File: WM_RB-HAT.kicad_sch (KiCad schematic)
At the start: 98 parts, among them J1 Line R, J2 Output Stereo, J3 2x20 Pins, J5 Output Mono, J7 Line L, Q1 BC817, Q2 BFS17A, U1 WM8960, U3 74AHC1G14, U4 MCP1711T-33 /OT, X1 XO32, Y1 24MHz

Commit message: WIP v1.1: SMD migration + input simplification
- Remove differential input stage, simplify jacks
- Migrate to 0603, remove HandSolder footprints
- Add LCSC codes, 4-layer stackup config
- Add SMD libs and design docs
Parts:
- removed C33, C34: 390p, Capacitor_SMD:C_0805_2012Metric_Pad1.18x1.45mm_HandSolder, symbol Device:C_Small
- removed C37, C38: 1u Film P5-7.5mm W<6mm, ArduinoModules:C_Rect_Film_L7.2mm_W5.5mm_P5.00mm_7.5mm_Combo_FKS2_FKP2_MKS2_MKP2, symbol Device:C_Small
- removed FB6, FB7: 220-1k, Inductor_SMD:L_0805_2012Metric_Pad1.15x1.40mm_HandSolder, symbol Device:FerriteBead_Small
- removed J1: Line R, ArduinoModules:Jack_3.5mm_Combo_CUI_SJ1-3525N_Horizontal, symbol Connector_Audio:AudioJack3_SwitchTR
- removed J2: Output Stereo, ArduinoModules:Jack_3.5mm_Combo_CUI_SJ1-3525N_Horizontal, symbol Connector_Audio:AudioJack3_SwitchTR
- removed J5: Output Mono, ArduinoModules:Jack_3.5mm_Combo_CUI_SJ1-3525N_Horizontal, symbol Connector_Audio:AudioJack3_SwitchTR
- removed J7: Line L, ArduinoModules:Jack_3.5mm_Combo_CUI_SJ1-3525N_Horizontal, symbol Connector_Audio:AudioJack3_SwitchTR
- removed JP3: Line, ArduinoModules:SolderJumper-2_P1.3mm_Open_TrianglePad1.0x1.5mm, symbol 0Arduino_Modules:SolderJumper_2_Open
- removed R25: 1k, Resistor_SMD:R_0805_2012Metric_Pad1.20x1.40mm_HandSolder, symbol Device:R_Small_US
- removed R28, R29: 100R, Resistor_SMD:R_0805_2012Metric_Pad1.20x1.40mm_HandSolder, symbol Device:R_Small_US
- removed R30, R31: 100K, Resistor_SMD:R_0805_2012Metric_Pad1.20x1.40mm_HandSolder, symbol Device:R_Small_US
- added J1, J2, J4, J5: AudioJack3, libs:AUDIO-SMD_PJ-320B, symbol Connector_Audio:AudioJack3
- C10: footprint Capacitor_SMD:C_0805_2012Metric_Pad1.18x1.45mm_HandSolder -> Capacitor_SMD:C_0603_1608Metric; LCSC (none) -> C14663
- C11, C13, C14, C15, C16, C17, C22: footprint ArduinoModules:C_1206_3216Metric_Pad1.33x1.80mm_HandSolder -> Capacitor_SMD:C_1206_3216Metric
- C12, C2, C21, C23, C24, C25, C29, C5, C7: footprint Capacitor_SMD:C_0805_2012Metric_Pad1.18x1.45mm_HandSolder -> Capacitor_SMD:C_0805_2012Metric
- C18, C19: value 1u Film P5-7.5mm W<6mm -> 1uF X7R; footprint ArduinoModules:C_Rect_Film_L7.2mm_W5.5mm_P5.00mm_7.5mm_Combo_FKS2_FKP2_MKS2_MKP2 -> Capacitor_SMD:C_0805_2012Metric; LCSC (none) -> C28323
- C20, C30, C9: footprint Capacitor_SMD:C_0805_2012Metric_Pad1.18x1.45mm_HandSolder -> Capacitor_SMD:C_0603_1608Metric; LCSC (none) -> C1603
- C26: footprint Capacitor_SMD:C_0805_2012Metric_Pad1.18x1.45mm_HandSolder -> Capacitor_SMD:C_0603_1608Metric; LCSC (none) -> C1646
- C27: footprint Capacitor_SMD:C_0805_2012Metric_Pad1.18x1.45mm_HandSolder -> Capacitor_SMD:C_0603_1608Metric; LCSC (none) -> C14858
- C28: footprint Capacitor_SMD:C_0805_2012Metric_Pad1.18x1.45mm_HandSolder -> Capacitor_SMD:C_0603_1608Metric; LCSC (none) -> C57112
- C3: footprint Capacitor_SMD:C_0805_2012Metric_Pad1.18x1.45mm_HandSolder -> Capacitor_SMD:C_0805_2012Metric; LCSC (none) -> C49678
- C31, C32, C8: footprint Capacitor_SMD:C_0805_2012Metric_Pad1.18x1.45mm_HandSolder -> Capacitor_SMD:C_0805_2012Metric; LCSC (none) -> C1779
- C35: footprint ArduinoModules:C_1206_3216Metric_Pad1.33x1.80mm_HandSolder -> Capacitor_SMD:C_1206_3216Metric; LCSC (none) -> C13585
- C36: value 1u Film P5mm W<6mm -> 1uF X7R; footprint Capacitor_THT:C_Rect_L7.2mm_W5.5mm_P5.00mm_FKS2_FKP2_MKS2_MKP2 -> Capacitor_SMD:C_0805_2012Metric; LCSC (none) -> C28323
- CP1, CP2, CP4: value 22-68uF Bipolar 25-35V -> 220uF 16V; footprint ArduinoModules:CP_Radial_D8.0mm_P2.50-3.5mm_100uF_Mejores_Pads -> libs:CAP-SMD_BD6.3-L6.6-W6.6-FD; LCSC (none) -> C90274
- CP3: value 100-470uF 6.3V -> 220uF 16V; footprint ArduinoModules:CP_Radial_D8.0mm_P2.50-3.5mm_100uF_Mejores_Pads -> libs:CAP-SMD_BD6.3-L6.6-W6.6-FD; LCSC (none) -> C90274
- FB1, FB2, FB3: footprint Inductor_SMD:L_0805_2012Metric_Pad1.15x1.40mm_HandSolder -> Inductor_SMD:L_0805_2012Metric; LCSC (none) -> C1029
- Q1: LCSC (none) -> C2137
- R1, R2, R26, R3, R4, R5: footprint Resistor_SMD:R_0805_2012Metric_Pad1.20x1.40mm_HandSolder -> Resistor_SMD:R_0603_1608Metric; LCSC (none) -> C22966
- R10, R24, R9: footprint Resistor_SMD:R_0805_2012Metric_Pad1.20x1.40mm_HandSolder -> Resistor_SMD:R_0805_2012Metric; LCSC (none) -> C17408
- R11: footprint ArduinoModules:R_1206_3216Metric_Pad1.30x1.75mm_HandSolder -> Resistor_SMD:R_1206_3216Metric
- R12, R15, R20: footprint Resistor_SMD:R_0805_2012Metric_Pad1.20x1.40mm_HandSolder -> Resistor_SMD:R_0603_1608Metric; LCSC (none) -> C21190
- R13, R16, R18: footprint Resistor_SMD:R_0805_2012Metric_Pad1.20x1.40mm_HandSolder -> Resistor_SMD:R_0603_1608Metric; LCSC (none) -> C23162
- R14, R17, R19, R21: footprint Resistor_SMD:R_0805_2012Metric_Pad1.20x1.40mm_HandSolder -> Resistor_SMD:R_0805_2012Metric
- R22, R6, R7, R8: footprint Resistor_SMD:R_0805_2012Metric_Pad1.20x1.40mm_HandSolder -> Resistor_SMD:R_0603_1608Metric; LCSC (none) -> C25803
- R23: footprint Resistor_SMD:R_0805_2012Metric_Pad1.20x1.40mm_HandSolder -> Resistor_SMD:R_0805_2012Metric; LCSC (none) -> C17407
- R27: footprint Resistor_SMD:R_0805_2012Metric_Pad1.20x1.40mm_HandSolder -> Resistor_SMD:R_0805_2012Metric; LCSC (none) -> C17168
- U1: footprint ArduinoModules:QFN-32-1EP_5x5mm_P0.5mm_EP3.3x3.3mm_Handsolder -> Package_DFN_QFN:QFN-32-1EP_5x5mm_P0.5mm_EP3.45x3.45mm; LCSC (none) -> C18752
- U3: footprint Package_TO_SOT_SMD:SOT-23-5_HandSoldering -> Package_TO_SOT_SMD:SOT-23-5
- U4: footprint Package_TO_SOT_SMD:TSOT-23-5_HandSoldering -> Package_TO_SOT_SMD:TSOT-23-5; LCSC (none) -> C79527
- X1: footprint Oscillator:Oscillator_SMD_EuroQuartz_XO32-4Pin_3.2x2.5mm_HandSoldering -> Oscillator:Oscillator_SMD_EuroQuartz_XO32-4Pin_3.2x2.5mm
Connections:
- net GND: now also J1.S, J2.S, J4.S, J5.S
- net HP_L_AC: now also J4.T
- net HP_R_AC: now also J4.R
- net OUT_MONO_AC: now also J2.R, J2.T
- net at FB1.1, JP1.1 (A): now also J1.R, J1.T
- net at FB2.1: now also J5.R, J5.T
- net GND_INPUT_L: no longer names the net of U1.4 (LINPUT1)
- net GND_INPUT_R: no longer names the net of U1.5 (RINPUT1)
- no-connect marks 33 -> 29
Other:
- moved on the sheet: C18, C19, C20, C21, FB1, FB2, JP1, R10, R15, R6, R7, R8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

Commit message: Fix ferrite bead LCSC code: C1029 → C85835
C1029 was a 3.3nH inductor (0603), not a ferrite bead.
C85835 is Murata BLM21AG102SN1D:
- 1kΩ @ 100MHz
- 0805 (matches footprint)
- 600mA rated
- Basic JLCPCB part

Affects FB1, FB2, FB3.
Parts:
- FB1, FB2, FB3: LCSC C1029 -> C85835
- J1: Label (none) -> INPUT_R
- J2: Label (none) -> OUTPUT_MONO
- J4: Label (none) -> OUTPUT_STEREO
- J5: Label (none) -> INPUT_L
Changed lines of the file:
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@@
 	(text "1V RMS 0dBV Output\n1kOhm minimum Load\n-3dB <10Hz"
 		(exclude_from_sim no)
-		(at 382.27 157.48 0)
+		(at 379.984 122.682 0)
 		(effects
 			(font
@@
 	(text "RLoad>10k for optimal THD"
 		(exclude_from_sim no)
-		(at 377.19 160.02 0)
+		(at 374.904 125.222 0)
 		(effects
 			(font
@@
 			)
 		)
-		(property "LCSC" "C14663"
-			(at 0 0 0)
+		(property "Description" ""
+			(at 148.59 245.11 0)
 			(effects
 				(font
@@
 			)
 		)
-		(property "Description" ""
-			(at 148.59 245.11 0)
+		(property "LCSC" "C14663"
+			(at 0 0 0)
 			(effects
 				(font
@@
 			)
 		)
-		(property "LCSC" "C57112"
-			(at 0 0 0)
+		(property "Description" ""
+			(at 96.52 241.3 0)
 			(effects
 				(font
@@
 			)
 		)
-		(property "Description" ""
-			(at 96.52 241.3 0)
+		(property "LCSC" "C57112"
+			(at 0 0 0)
 			(effects
 				(font
@@
 		(on_board yes)
 		(dnp no)
-		(fields_autoplaced yes)
 		(property "Reference" "J2"
 			(at 394.97 174.6249 0)
@@
 			)
 		)
+		(property "Label" "OUTPUT_MONO"
+			(at 391.16 181.864 0)
+			(effects
+				(font
+					(size 1.27 1.27)
+				)
+			)
+		)
 		(pin "R"
 		)
@@
 			)
 		)
-		(property "LCSC" "C23162"
-			(at 0 0 0)
+		(property "Description" ""
+			(at 64.77 271.78 0)
 			(effects
 				(font
@@
 			)
 		)
-		(property "Description" ""
-			(at 64.77 271.78 0)
+		(property "LCSC" "C23162"
+			(at 0 0 0)
 			(effects
 				(font
@@
 		(on_board yes)
 		(dnp no)
-		(fields_autoplaced yes)
 		(property "Reference" "J5"
 			(at 27.94 166.2429 0)
@@
 			)
 		)
+		(property "Label" "INPUT_L"
+			(at 23.876 171.196 0)
+			(effects
+				(font
+					(size 1.27 1.27)
+				)
+			)
+		)
 		(pin "R"
 		)
@@
 			)
 		)
-		(property "LCSC" "C23162"
-			(at 0 0 0)
+		(property "Description" ""
+			(at 53.34 256.54 0)
 			(effects
 				(font
@@
 			)
 		)
-		(property "Description" ""
-			(at 53.34 256.54 0)
+		(property "LCSC" "C23162"
+			(at 0 0 0)
 			(effects
 				(font
@@
 			)
 		)
-		(property "LCSC" "C25803"
-			(at 0 0 0)
+		(property "Description" ""
+			(at 378.46 180.34 0)
 			(effects
 				(font
@@
 			)
 		)
-		(property "Description" ""
-			(at 378.46 180.34 0)
+		(property "LCSC" "C25803"
+			(at 0 0 0)
 			(effects
 				(font
@@
 			)
 		)
-		(property "LCSC" "C1603"
-			(at 0 0 0)
+		(property "Description" ""
+			(at 369.57 180.34 0)
 			(effects
 				(font
@@
 			)
 		)
-		(property "Description" ""
-			(at 369.57 180.34 0)
+		(property "LCSC" "C1603"
+			(at 0 0 0)
 			(effects
 				(font
@@
 			)
 		)
-		(property "LCSC" "C1029"
+		(property "LCSC" "C85835"
 			(at 48.26 144.272 0)
 			(effects
@@
 			)
 		)
-		(property "LCSC" "C23162"
-			(at 0 0 0)
+		(property "Description" ""
+			(at 172.72 22.86 0)
 			(effects
 				(font
@@
 			)
 		)
-		(property "Description" ""
-			(at 172.72 22.86 0)
+		(property "LCSC" "C23162"
+			(at 0 0 0)
 			(effects
 				(font
@@
 			)
 		)
-		(property "LCSC" "C1646"
-			(at 0 0 0)
+		(property "Description" ""
+			(at 24.13 265.43 0)
 			(effects
 				(font
@@
 			)
 		)
-		(property "Description" ""
-			(at 24.13 265.43 0)
+		(property "LCSC" "C1646"
+			(at 0 0 0)
 			(effects
 				(font
@@
 			)
 		)
-		(property "LCSC" "C14858"
-			(at 0 0 0)
+		(property "Description" ""
+			(at 30.48 260.35 0)
 			(effects
 				(font
@@
 			)
 		)
-		(property "Description" ""
-			(at 30.48 260.35 0)
+		(property "LCSC" "C14858"
+			(at 0 0 0)
 			(effects
 				(font
@@
 			)
 		)
-		(property "LCSC" "C1029"
+		(property "LCSC" "C85835"
 			(at 40.64 59.69 0)
 			(effects
@@
 			)
 		)
-		(property "LCSC" "C1029"
+		(property "LCSC" "C85835"
 			(at 48.26 168.148 0)
 			(effects
@@
 			)
 		)
-		(property "LCSC" "C22966"
-			(at 0 0 0)
+		(property "Description" ""
+			(at 181.61 43.18 0)
 			(effects
 				(font
@@
 			)
 		)
-		(property "Description" ""
-			(at 181.61 43.18 0)
+		(property "LCSC" "C22966"
+			(at 0 0 0)
 			(effects
 				(font
@@
 			)
 		)
-		(property "LCSC" "C25803"
-			(at 0 0 0)
+		(property "Description" ""
+			(at 378.46 146.05 0)
 			(effects
 				(font
@@
 			)
 		)
-		(property "Description" ""
-			(at 378.46 146.05 0)
+		(property "LCSC" "C25803"
+			(at 0 0 0)
 			(effects
 				(font
@@
 		(on_board yes)
 		(dnp no)
-		(fields_autoplaced yes)
 		(property "Reference" "J4"
 			(at 394.97 137.7949 0)
@@
 			)
 		)
+		(property "Label" "OUTPUT_STEREO"
+			(at 392.176 145.288 0)
+			(effects
+				(font
+					(size 1.27 1.27)
+				)
+			)
+		)
 		(pin "R"
 		)
@@
 		(on_board yes)
 		(dnp no)
-		(fields_autoplaced yes)
 		(property "Reference" "J1"
 			(at 27.94 142.3669 0)
@@
 			)
 		)
+		(property "Label" "INPUT_R"
+			(at 23.876 147.32 0)
+			(effects
+				(font
+					(size 1.27 1.27)
+				)
+			)
+		)
 		(pin "R"
 		)
@@
 			)
 		)
-		(property "LCSC" "C21190"
-			(at 0 0 0)
+		(property "Description" ""
+			(at 39.37 248.92 0)
 			(effects
 				(font
@@
 			)
 		)
-		(property "Description" ""
-			(at 39.37 248.92 0)
+		(property "LCSC" "C21190"
+			(at 0 0 0)
 			(effects
 				(font

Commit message: Add missing LCSC codes for JLCPCB assembly
Components added:
- C2 (4.7u 0805): C1779
- C5 (100n 0805): C49678
- C7,C21,C29 (390p 0805): C1671
- C22 (47u 1206): C96123
- J1,J2,J4,J5 (PJ-320B): C18594
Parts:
- C2: LCSC (none) -> C1779
- C21, C29, C7: LCSC (none) -> C1671
- C22: LCSC (none) -> C96123
- C5: LCSC (none) -> C49678
- J1, J2, J4, JP1: LCSC (none) -> C18594
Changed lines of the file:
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@@
 			)
 		)
+		(property "LCSC" "C1779"
+			(at 0 0 0)
+			(effects
+				(font
+					(size 1.27 1.27)
+				)
+				(hide yes)
+			)
+		)
 		(pin "1"
 		)
@@
 			)
 		)
+		(property "LCSC" "C49678"
+			(at 0 0 0)
+			(effects
+				(font
+					(size 1.27 1.27)
+				)
+				(hide yes)
+			)
+		)
 		(pin "1"
 		)
@@
 			)
 		)
+		(property "LCSC" "C1671"
+			(at 0 0 0)
+			(effects
+				(font
+					(size 1.27 1.27)
+				)
+				(hide yes)
+			)
+		)
 		(pin "1"
 		)
@@
 			)
 		)
+		(property "LCSC" "C18594"
+			(at 0 0 0)
+			(effects
+				(font
+					(size 1.27 1.27)
+				)
+				(hide yes)
+			)
+		)
 		(pin "R"
 		)
@@
 			)
 		)
+		(property "LCSC" "C18594"
+			(at 0 0 0)
+			(effects
+				(font
+					(size 1.27 1.27)
+				)
+				(hide yes)
+			)
+		)
 		(pin "1"
 		)
@@
 			)
 		)
+		(property "LCSC" "C1671"
+			(at 0 0 0)
+			(effects
+				(font
+					(size 1.27 1.27)
+				)
+				(hide yes)
+			)
+		)
 		(pin "1"
 		)
@@
 			)
 		)
+		(property "LCSC" "C96123"
+			(at 0 0 0)
+			(effects
+				(font
+					(size 1.27 1.27)
+				)
+				(hide yes)
+			)
+		)
 		(pin "1"
 		)
@@
 			)
 		)
+		(property "LCSC" "C1671"
+			(at 0 0 0)
+			(effects
+				(font
+					(size 1.27 1.27)
+				)
+				(hide yes)
+			)
+		)
 		(pin "1"
 		)
@@
 			)
 		)
+		(property "LCSC" "C18594"
+			(at 0 0 0)
+			(effects
+				(font
+					(size 1.27 1.27)
+				)
+				(hide yes)
+			)
+		)
 		(pin "R"
 		)
@@
 			)
 		)
+		(property "LCSC" "C18594"
+			(at 0 0 0)
+			(effects
+				(font
+					(size 1.27 1.27)
+				)
+				(hide yes)
+			)
+		)

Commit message: WIP: 4-layer SIG/GND/GND/SIG stackup + SMD migration progress
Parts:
- removed FM1, FM2, FM3: Fiducial, ArduinoModules:Fiducial_1mm_Mask2mm, symbol Mechanical:Fiducial
- added J6: Audio In, Connector_PinHeader_2.54mm:PinHeader_1x04_P2.54mm_Vertical, symbol Connector:Conn_01x04_Pin
- added J7: Audio Out, Connector_PinHeader_2.54mm:PinHeader_1x04_P2.54mm_Vertical, symbol Connector:Conn_01x04_Pin
- C12: footprint Capacitor_SMD:C_0805_2012Metric -> Capacitor_SMD:C_0603_1608Metric; LCSC (none) -> C21122
- C20, C30, C9: LCSC C1603 -> C1617
- C21, C29, C7: footprint Capacitor_SMD:C_0805_2012Metric -> Capacitor_SMD:C_0603_1608Metric; LCSC C1671 -> C1617
- C23: footprint Capacitor_SMD:C_0805_2012Metric -> Capacitor_SMD:C_0603_1608Metric; LCSC (none) -> C14663
- C24: footprint Capacitor_SMD:C_0805_2012Metric -> Capacitor_SMD:C_0603_1608Metric; LCSC (none) -> C57112
- C25: footprint Capacitor_SMD:C_0805_2012Metric -> Capacitor_SMD:C_0603_1608Metric; LCSC (none) -> C1647
- C26: LCSC C1646 -> C1647
- C3, C5: footprint Capacitor_SMD:C_0805_2012Metric -> Capacitor_SMD:C_0603_1608Metric; LCSC C49678 -> C14663
- R10, R24, R9: footprint Resistor_SMD:R_0805_2012Metric -> Resistor_SMD:R_0603_1608Metric; LCSC C17408 -> C22775
- R14, R17, R19: footprint Resistor_SMD:R_0805_2012Metric -> Resistor_SMD:R_0603_1608Metric; LCSC (none) -> C23162
- R21: footprint Resistor_SMD:R_0805_2012Metric -> Resistor_SMD:R_0603_1608Metric; LCSC (none) -> C22966
- R23: footprint Resistor_SMD:R_0805_2012Metric -> Resistor_SMD:R_0603_1608Metric; LCSC C17407 -> C25803
- R27: footprint Resistor_SMD:R_0805_2012Metric -> Resistor_SMD:R_0603_1608Metric; LCSC C17168 -> C21189
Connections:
- net GND: now also J6.1 (Pin_1), J6.3 (Pin_3), J7.1 (Pin_1), J7.3 (Pin_3)
- net INPUT_L: now reaches FB2.1, J5.R, J5.T
- net INPUT_L: now also J6.4 (Pin_4)
- net INPUT_R: now reaches FB1.1, J1.R, J1.T, JP1.1 (A)
- net INPUT_R: now also J6.2 (Pin_2)
- new net OUTPUT_L: J7.4 (Pin_4)
- new net OUTPUT_R: J7.2 (Pin_2)
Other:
- moved on the sheet: C18, C19, C20, C21, FB1, FB2, J1, J5, JP1, R10, R15, R7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

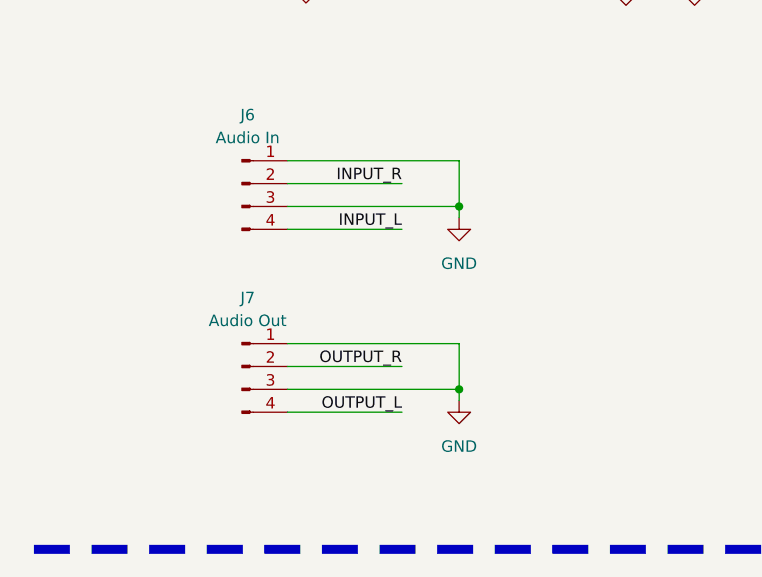
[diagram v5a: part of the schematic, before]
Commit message: Rename audio I/O labels (LINE_INPUT, HP_AC)
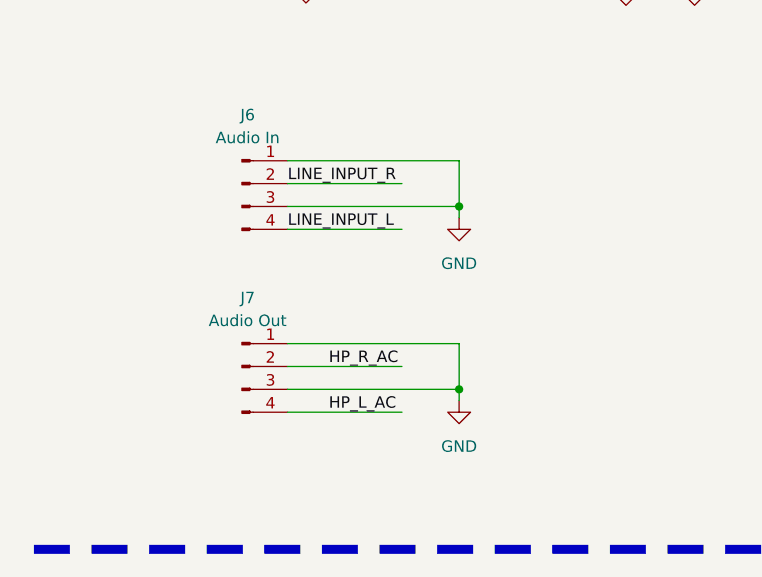
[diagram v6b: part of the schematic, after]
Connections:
- net OUTPUT_L is gone; now on net HP_L_AC: J7.4 (Pin_4)
- net OUTPUT_R is gone; now on net HP_R_AC: J7.2 (Pin_2)
- net INPUT_L: no longer J6.4 (Pin_4)
- net INPUT_R: no longer J6.2 (Pin_2)
- net LINE_INPUT_L: now also J6.4 (Pin_4)
- net LINE_INPUT_R: now also J6.2 (Pin_2)
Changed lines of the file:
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@@
+		)
+	)
+	(label "HP_R_AC"
+		(at 45.466 198.12 0)
+		(effects
+			(font
+				(size 1.27 1.27)
+			)
+			(justify left bottom)
 		)
 	)
@@
 		)
 	)
+	(label "HP_L_AC"
+		(at 45.466 203.2 0)
+		(effects
+			(font
+				(size 1.27 1.27)
+			)
+			(justify left bottom)
+		)
+	)
 	(label "I2C_SCL"
 		(at 170.18 40.64 0)
@@
 		)
 	)
+	(label "LINE_INPUT_R"
+		(at 40.894 177.8 0)
+		(effects
+			(font
+				(size 1.27 1.27)
+			)
+			(justify left bottom)
+		)
+	)
 	(label "P3V3_HAT"
 		(at 172.72 19.05 0)
@@
 		)
 	)
-	(label "INPUT_R"
-		(at 53.594 177.8 180)
-		(effects
-			(font
-				(size 1.27 1.27)
-			)
-			(justify right bottom)
-		)
-	)
-	(label "INPUT_L"
-		(at 53.594 182.88 180)
-		(effects
-			(font
-				(size 1.27 1.27)
-			)
-			(justify right bottom)
-		)
-	)
 	(label "P3V3_HAT"
 		(at 170.18 35.56 0)
@@
 		)
 	)
+	(label "LINE_INPUT_L"
+		(at 40.894 182.88 0)
+		(effects
+			(font
+				(size 1.27 1.27)
+			)
+			(justify left bottom)
+		)
+	)
 	(label "I2C_SDA"
 		(at 246.38 172.72 180)
@@
 		)
 	)
-	(label "OUTPUT_L"
-		(at 53.594 203.2 180)
-		(effects
-			(font
-				(size 1.27 1.27)
-			)
-			(justify right bottom)
-		)
-	)
 	(label "I2S_ADC"
 		(at 181.61 210.82 0)
@@
 			)
 			(justify right bottom)
-		)
-	)
-	(label "OUTPUT_R"
-		(at 53.594 198.12 180)
-		(effects
-			(font
-				(size 1.27 1.27)
-			)
-			(justify right bottom)
